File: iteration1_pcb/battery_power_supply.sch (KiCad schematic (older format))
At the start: 15 parts, among them U6 LMR50410XFDBVR, U7 MIC5504-3.3YM5

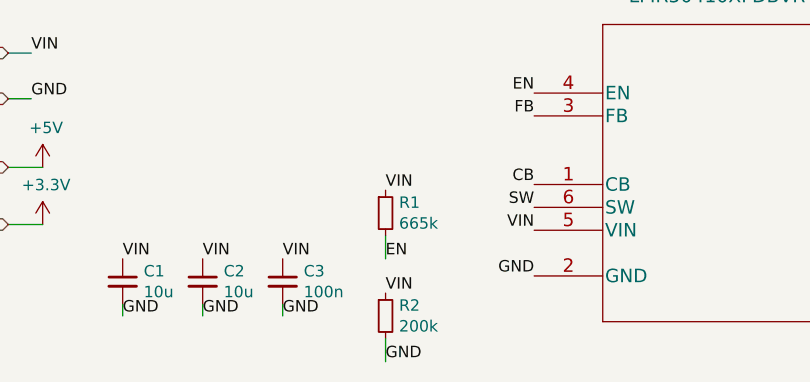
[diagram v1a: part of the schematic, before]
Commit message: Adding schematic work
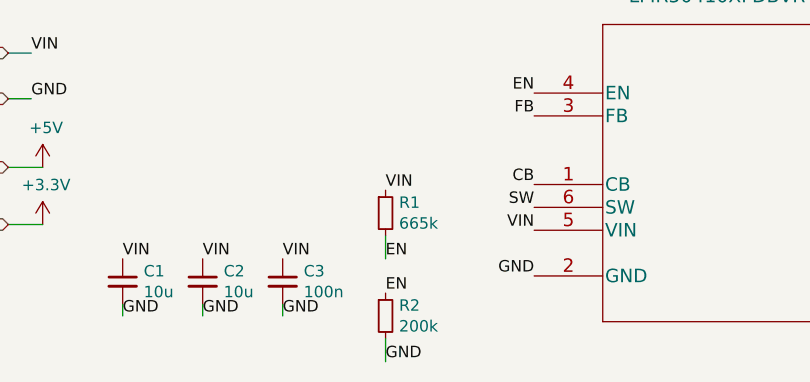
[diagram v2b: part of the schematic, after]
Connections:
- net EN: now also R2.1
- net VIN: no longer R2.1
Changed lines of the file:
@@
 $EndComp
 Text Label 4150 3750 0    50   ~ 0
-VIN
+EN
 Text Label 4150 4050 0    50   ~ 0
 GND
